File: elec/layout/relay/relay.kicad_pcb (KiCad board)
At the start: 4 copper layers, 6 parts

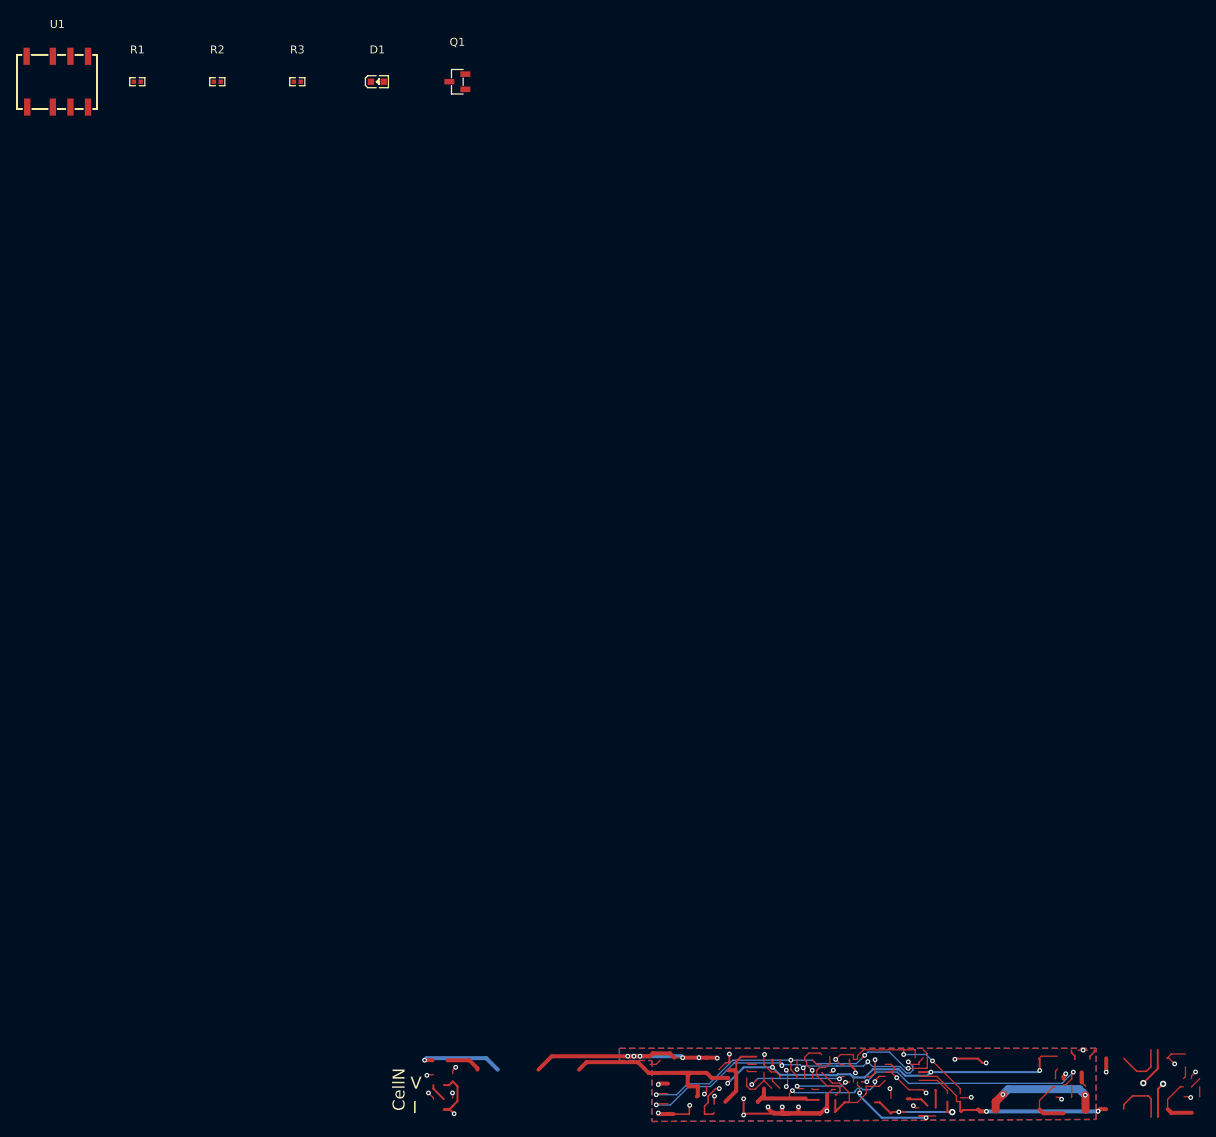
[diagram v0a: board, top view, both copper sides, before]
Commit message: update relay layout
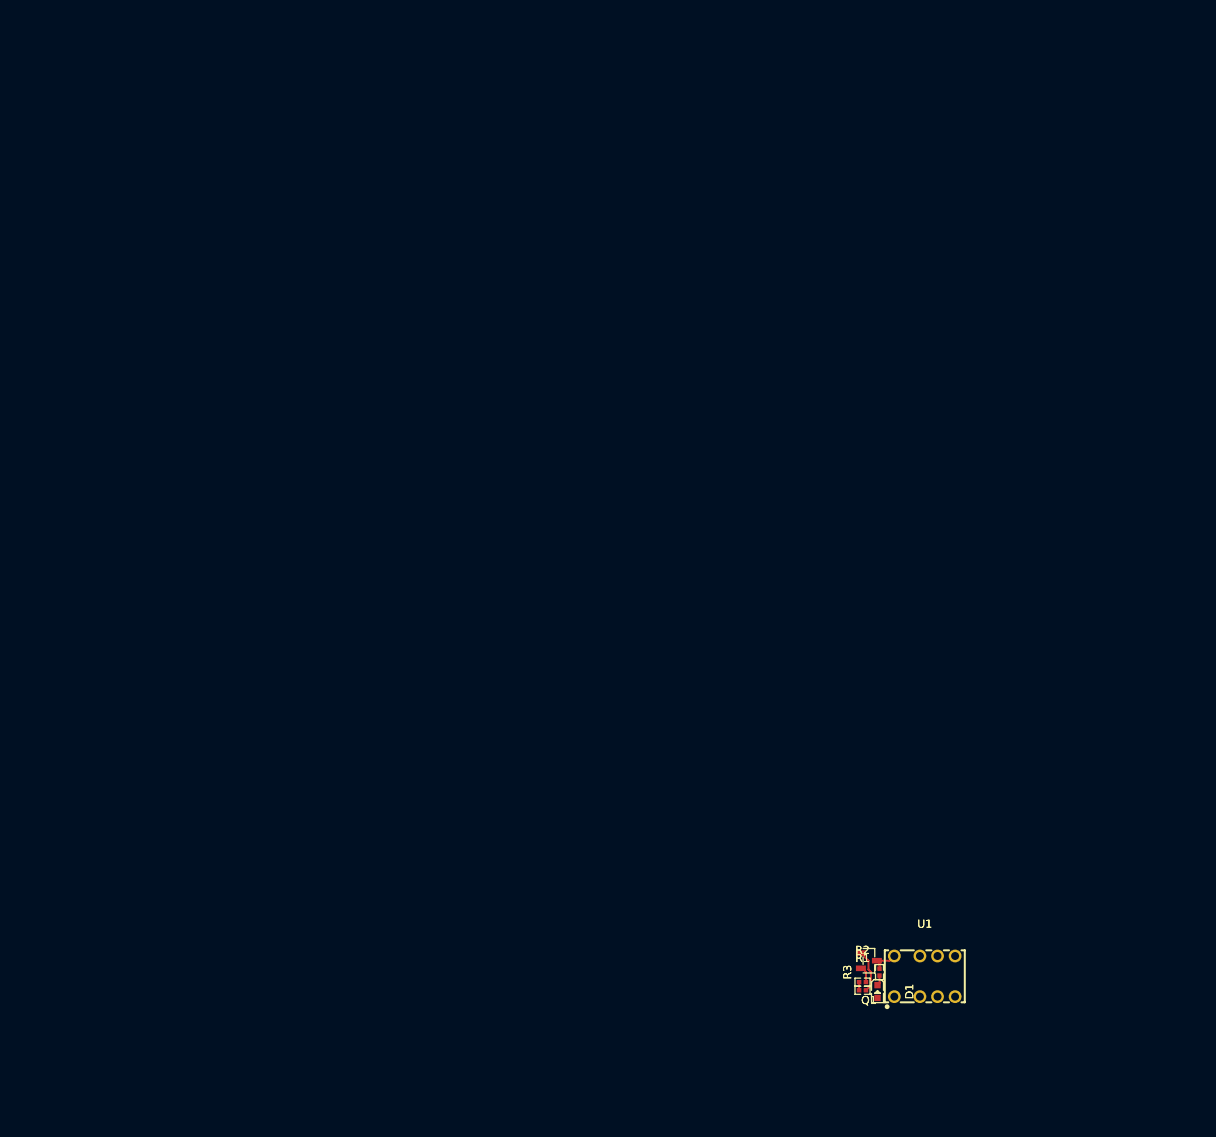
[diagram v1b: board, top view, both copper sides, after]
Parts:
- U1: footprint lib:RELAY-SMD_HFD4-5-SR -> atopile:RELAY-TH_HFDXXX-689a1e
- moved U1 155.8 mm to (118.4, 106.8)
- moved R1 145.3 mm to (110.7, 108.6)
- moved R2 138.5 mm to (110.7, 107.5)
- moved R3 133.0 mm to (112.8, 106.3), turned to 90 degrees
- moved D1 129.8 mm to (112.5, 108.7), turned to -90 degrees
- moved Q1 121.3 mm to (111.5, 104.9), turned to 180 degrees
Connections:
- D1 pad 2: hv -> anode
- Q1 pad 2: gnd-3 -> gnd-2
- Q1 pad 3: gnd-2 -> gnd
- R2 pad 2: gnd-3 -> gnd-2
- R3 pad 2: gnd-2 -> gnd
- U1 pad 1: hv -> anode
- U1 pad 2: (no net) -> relay.footprint.pins[1].net-net
- U1 pad 3: gnd -> gnd-3
- U1 pad 5: hv-2 -> hv
- U1 pad 7: (no net) -> relay.footprint.pins[6].net-net
- U1 pad 8: gnd-2 -> gnd
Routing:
- net (no net): track 617.3 -> 0.00 mm, vias 81 -> 0
- net gate: track 0.00 -> 5.42 mm
- net gnd: track 0.00 -> 3.88 mm
- net gnd-2: track 0.00 -> 2.16 mm
- net cathode: track 0.00 -> 1.30 mm
- net line: track 0.00 -> 1.03 mm
- removed copper zone on B.Cu, net (none)
- removed copper zone on F.Cu, net (none)
- removed copper zone on In1.Cu, net (none)
- removed copper zone on In2.Cu, net (none)
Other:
- board text removed: "CellN"
- board text removed: "I"
- board text removed: "V"

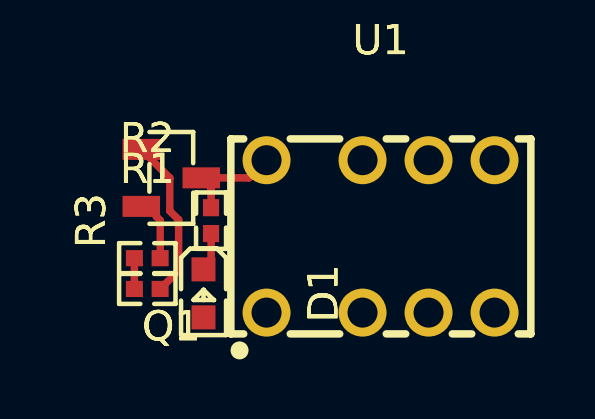
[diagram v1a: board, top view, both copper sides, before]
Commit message: update layouts to kicad 9
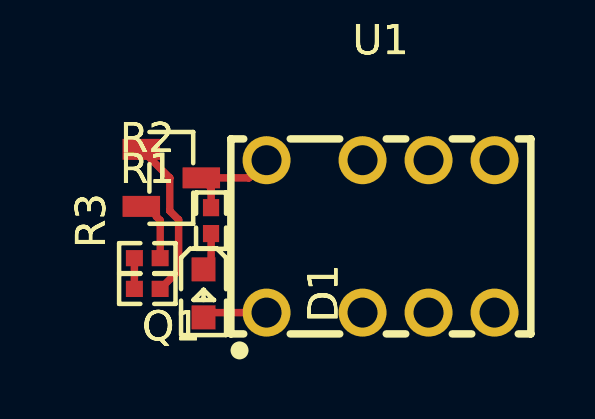
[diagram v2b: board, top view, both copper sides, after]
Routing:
- net anode: track 0.00 -> 2.17 mm

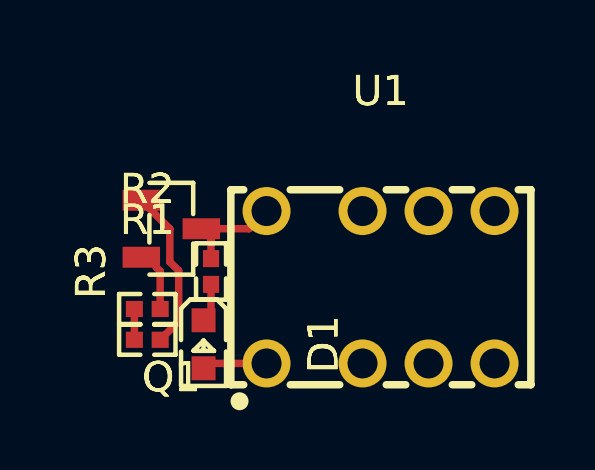
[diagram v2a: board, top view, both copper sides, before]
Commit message: update n-fet part for stock
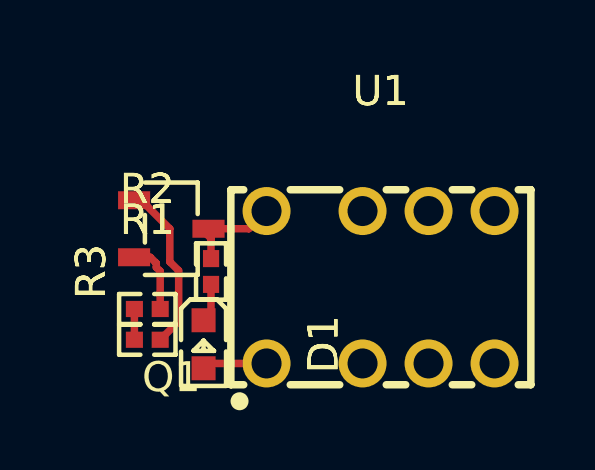
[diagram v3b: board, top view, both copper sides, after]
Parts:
- Q1: footprint atopile:SOT-23-3_L2.9-W1.3-P1.90-LS2.4-BR-688f29 -> atopile:SOT-23-3_L2.9-W1.6-P1.90-LS2.8-BR-186170
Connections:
- Q1 pad 2: gnd-2 -> gnd-1
- R2 pad 2: gnd-2 -> gnd-1
- U1 pad 3: gnd-3 -> gnd-2
- U1 pad 4: gnd-1 -> gnd-3
- U1 pad 5: hv -> hv-1
- U1 pad 6: hv-1 -> hv
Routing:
- net gnd-2: track 2.16 -> 0.00 mm
- net gnd-1: track 0.00 -> 2.16 mm

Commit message: building frozen
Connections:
- D1 pad 2: anode -> hv-1
- Q1 pad 2: gnd-1 -> gnd-2
- Q1 pad 3: gnd -> gnd-1
- R2 pad 2: gnd-1 -> gnd-2
- R3 pad 2: gnd -> gnd-1
- U1 pad 1: anode -> hv-1
- U1 pad 3: gnd-2 -> gnd-3
- U1 pad 4: gnd-3 -> gnd
- U1 pad 5: hv-1 -> hv-2
- U1 pad 8: gnd -> gnd-1
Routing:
- net gnd: track 3.88 -> 0.00 mm
- net hv-1: track 0.00 -> 2.17 mm
- net anode: track 2.17 -> 0.00 mm
- net gnd-2: track 0.00 -> 2.16 mm
- net gnd-1: track 2.16 -> 3.88 mm
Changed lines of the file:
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@@
         (legacy_teardrops no)
     )
-    (paper A4)
+    (paper "A4")
     (layers
         (0 "F.Cu" signal)
@@
         (tenting front back)
         (pcbplotparams
-            (layerselection "0x00000000_00000000_55555555_5755f5ff")
-            (plot_on_all_layers_selection "0x00000000_00000000_00000000_00000000")
+            (layerselection 0x00000000_00000000_55555555_5755f5ff)
+            (plot_on_all_layers_selection 0x00000000_00000000_00000000_00000000)
             (disableapertmacros no)
             (usegerberextensions no)
@@
             (dxfusepcbnewfont yes)
             (psnegative no)
+            (psa4output no)
             (plot_black_and_white yes)
-            (psa4output no)
+            (plotinvisibletext no)
+            (sketchpadsonfab no)
             (plotreference yes)
+            (plotvalue yes)
             (plotpadnumbers no)
             (hidednponfab no)
             (sketchdnponfab yes)
             (crossoutdnponfab yes)
-            (plotvalue yes)
             (plotfptext yes)
-            (plotinvisibletext no)
-            (sketchpadsonfab no)
             (subtractmaskfromsilk no)
             (outputformat 1)
@@
     )
     (net 0 "")
-    (net 1 "gnd-3")
-    (net 2 "gnd-1")
+    (net 1 "gnd")
+    (net 2 "gnd-2")
     (net 3 "hv")
-    (net 4 "gnd-2")
-    (net 5 "hv-1")
+    (net 4 "gnd-3")
+    (net 5 "hv-2")
     (net 6 "cathode")
-    (net 7 "gnd")
-    (net 8 "anode")
+    (net 7 "gnd-1")
+    (net 8 "hv-1")
     (net 9 "gate")
     (net 10 "line")
@@
             (size 0.57 0.54)
             (layers "F.Cu" "F.Mask" "F.Paste")
-            (net 2 "gnd-1")
+            (net 2 "gnd-2")
             (remove_unused_layers yes)
             (keep_end_layers yes)
@@
             (size 0.57 0.54)
             (layers "F.Cu" "F.Mask" "F.Paste")
-            (net 7 "gnd")
+            (net 7 "gnd-1")
             (remove_unused_layers yes)
             (keep_end_layers yes)
@@
             (size 0.8 0.8)
             (layers "F.Cu" "F.Mask" "F.Paste")
-            (net 8 "anode")
+            (net 8 "hv-1")
             (remove_unused_layers yes)
             (keep_end_layers yes)
@@
             (drill 0.999998)
             (layers "*.Cu" "*.Mask")
-            (net 8 "anode")
+            (net 8 "hv-1")
             (remove_unused_layers no)
             (keep_end_layers yes)
@@
             (drill 0.999998)
             (layers "*.Cu" "*.Mask")
-            (net 4 "gnd-2")
+            (net 4 "gnd-3")
             (remove_unused_layers no)
             (keep_end_layers yes)
@@
             (drill 0.999998)
             (layers "*.Cu" "*.Mask")
-            (net 1 "gnd-3")
+            (net 1 "gnd")
             (remove_unused_layers no)
             (keep_end_layers yes)
@@
             (drill 0.999998)
             (layers "*.Cu" "*.Mask")
-            (net 5 "hv-1")
+            (net 5 "hv-2")
             (remove_unused_layers no)
             (keep_end_layers yes)
@@
             (drill 0.999998)
             (layers "*.Cu" "*.Mask")
-            (net 7 "gnd")
+            (net 7 "gnd-1")
             (remove_unused_layers no)
             (keep_end_layers yes)
@@
             (size 1.07 0.6)
             (layers "F.Cu" "F.Paste" "F.Mask")
-            (net 2 "gnd-1")
+            (net 2 "gnd-2")
             (remove_unused_layers yes)
             (keep_end_layers yes)
@@
             (size 1.07 0.6)
             (layers "F.Cu" "F.Paste" "F.Mask")
-            (net 7 "gnd")
+            (net 7 "gnd-1")
             (remove_unused_layers yes)
             (keep_end_layers yes)

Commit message: Build everything with ordered params to fix frozen builds
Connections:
- Q1 pad 2: gnd-2 -> gnd
- R2 pad 2: gnd-2 -> gnd
- U1 pad 4: gnd -> gnd-2
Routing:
- net gnd-2: track 2.16 -> 0.00 mm
- net gnd: track 0.00 -> 2.16 mm
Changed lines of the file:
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@@
     )
     (net 0 "")
-    (net 1 "gnd")
-    (net 2 "gnd-2")
+    (net 1 "gnd-2")
+    (net 2 "gnd")
     (net 3 "hv")
     (net 4 "gnd-3")
@@
             )
         )
+        (property "PARAM_max_power" "{\"type\": \"Quantity_Set_Discrete\", \"data\": {\"intervals\": {\"type\": \"Numeric_Interval_Disjoint\", \"data\": {\"intervals\": [{\"type\": \"Numeric_Interval\", \"data\": {\"min\": 0.0625, \"max\": 0.0625}}]}}, \"unit\": \"watt\"}}"
+            (at 0 0 0)
+            (layer "User.9")
+            (hide yes)
+            (effects
+                (font
+                    (size 0.125 0.125)
+                    (thickness 0.01875)
+                )
+            )
+        )
+        (property "PARAM_resistance" "{\"type\": \"Quantity_Interval_Disjoint\", \"data\": {\"intervals\": {\"type\": \"Numeric_Interval_Disjoint\", \"data\": {\"intervals\": [{\"type\": \"Numeric_Interval\", \"data\": {\"min\": 990.0000002235174, \"max\": 1009.9999997764826}}]}}, \"unit\": \"ohm\"}}"
+            (at 0 0 0)
+            (layer "User.9")
+            (hide yes)
+            (effects
+                (font
+                    (size 0.125 0.125)
+                    (thickness 0.01875)
+                )
+            )
+        )
+        (property "PARAM_max_voltage" "{\"type\": \"Quantity_Set_Discrete\", \"data\": {\"intervals\": {\"type\": \"Numeric_Interval_Disjoint\", \"data\": {\"intervals\": [{\"type\": \"Numeric_Interval\", \"data\": {\"min\": 50.0, \"max\": 50.0}}]}}, \"unit\": \"volt\"}}"
+            (at 0 0 0)
+            (layer "User.9")
+            (hide yes)
+            (effects
+                (font
+                    (size 0.125 0.125)
+                    (thickness 0.01875)
+                )
+            )
+        )
         (attr smd)
         (fp_line
@@
             (size 0.57 0.54)
             (layers "F.Cu" "F.Mask" "F.Paste")
-            (net 2 "gnd-2")
+            (net 2 "gnd")
             (remove_unused_layers yes)
             (keep_end_layers yes)
@@
             )
         )
+        (property "PARAM_max_power" "{\"type\": \"Quantity_Set_Discrete\", \"data\": {\"intervals\": {\"type\": \"Numeric_Interval_Disjoint\", \"data\": {\"intervals\": [{\"type\": \"Numeric_Interval\", \"data\": {\"min\": 0.0625, \"max\": 0.0625}}]}}, \"unit\": \"watt\"}}"
+            (at 0 0 0)
+            (layer "User.9")
+            (hide yes)
+            (effects
+                (font
+                    (size 0.125 0.125)
+                    (thickness 0.01875)
+                )
+            )
+        )
+        (property "PARAM_resistance" "{\"type\": \"Quantity_Interval_Disjoint\", \"data\": {\"intervals\": {\"type\": \"Numeric_Interval_Disjoint\", \"data\": {\"intervals\": [{\"type\": \"Numeric_Interval\", \"data\": {\"min\": 9900.000002235174, \"max\": 10099.999997764826}}]}}, \"unit\": \"ohm\"}}"
+            (at 0 0 0)
+            (layer "User.9")
+            (hide yes)
+            (effects
+                (font
+                    (size 0.125 0.125)
+                    (thickness 0.01875)
+                )
+            )
+        )
+        (property "PARAM_max_voltage" "{\"type\": \"Quantity_Set_Discrete\", \"data\": {\"intervals\": {\"type\": \"Numeric_Interval_Disjoint\", \"data\": {\"intervals\": [{\"type\": \"Numeric_Interval\", \"data\": {\"min\": 50.0, \"max\": 50.0}}]}}, \"unit\": \"volt\"}}"
+            (at 0 0 0)
+            (layer "User.9")
+            (hide yes)
+            (effects
+                (font
+                    (size 0.125 0.125)
+                    (thickness 0.01875)
+                )
+            )
+        )
         (attr smd)
         (fp_line
@@
             )
         )
+        (property "PARAM_max_power" "{\"type\": \"Quantity_Set_Discrete\", \"data\": {\"intervals\": {\"type\": \"Numeric_Interval_Disjoint\", \"data\": {\"intervals\": [{\"type\": \"Numeric_Interval\", \"data\": {\"min\": 0.0625, \"max\": 0.0625}}]}}, \"unit\": \"watt\"}}"
+            (at 0 0 0)
+            (layer "User.9")
+            (hide yes)
+            (effects
+                (font
+                    (size 0.125 0.125)
+                    (thickness 0.01875)
+                )
+            )
+        )
+        (property "PARAM_resistance" "{\"type\": \"Quantity_Interval_Disjoint\", \"data\": {\"intervals\": {\"type\": \"Numeric_Interval_Disjoint\", \"data\": {\"intervals\": [{\"type\": \"Numeric_Interval\", \"data\": {\"min\": 990.0000002235174, \"max\": 1009.9999997764826}}]}}, \"unit\": \"ohm\"}}"
+            (at 0 0 0)
+            (layer "User.9")
+            (hide yes)
+            (effects
+                (font
+                    (size 0.125 0.125)
+                    (thickness 0.01875)
+                )
+            )
+        )
+        (property "PARAM_max_voltage" "{\"type\": \"Quantity_Set_Discrete\", \"data\": {\"intervals\": {\"type\": \"Numeric_Interval_Disjoint\", \"data\": {\"intervals\": [{\"type\": \"Numeric_Interval\", \"data\": {\"min\": 50.0, \"max\": 50.0}}]}}, \"unit\": \"volt\"}}"
+            (at 0 0 0)
+            (layer "User.9")
+            (hide yes)
+            (effects
+                (font
+                    (size 0.125 0.125)
+                    (thickness 0.01875)
+                )
+            )
+        )
         (attr smd)
         (fp_line
@@
             (drill 0.999998)
             (layers "*.Cu" "*.Mask")
-            (net 1 "gnd")
+            (net 1 "gnd-2")
             (remove_unused_layers no)
             (keep_end_layers yes)
@@
             (size 1.07 0.6)
             (layers "F.Cu" "F.Paste" "F.Mask")
-            (net 2 "gnd-2")
+            (net 2 "gnd")
             (remove_unused_layers yes)
             (keep_end_layers yes)

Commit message: Cleanup layout for usb hub and usb-uart, add CM5 controller heatsink outline
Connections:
- D1 pad 2: hv-1 -> hv-2
- U1 pad 1: hv-1 -> hv-2
- U1 pad 5: hv-2 -> hv-1
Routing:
- net hv-2: track 0.00 -> 2.17 mm
- net hv-1: track 2.17 -> 0.00 mm
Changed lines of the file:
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@@
     (net 3 "hv")
     (net 4 "gnd-3")
-    (net 5 "hv-2")
+    (net 5 "hv-1")
     (net 6 "cathode")
     (net 7 "gnd-1")
-    (net 8 "hv-1")
+    (net 8 "hv-2")
     (net 9 "gate")
     (net 10 "line")
@@
             (size 0.8 0.8)
             (layers "F.Cu" "F.Mask" "F.Paste")
-            (net 8 "hv-1")
+            (net 8 "hv-2")
             (remove_unused_layers yes)
             (keep_end_layers yes)
@@
             (drill 0.999998)
             (layers "*.Cu" "*.Mask")
-            (net 8 "hv-1")
+            (net 8 "hv-2")
             (remove_unused_layers no)
             (keep_end_layers yes)
@@
             (drill 0.999998)
             (layers "*.Cu" "*.Mask")
-            (net 5 "hv-2")
+            (net 5 "hv-1")
             (remove_unused_layers no)
             (keep_end_layers yes)

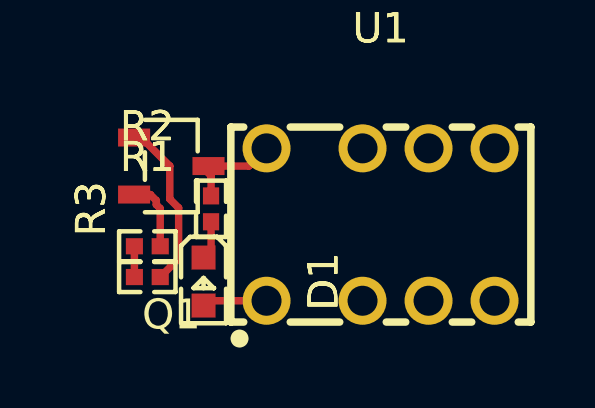
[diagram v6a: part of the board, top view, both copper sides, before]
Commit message: update address pin on analog out, update led value on relay
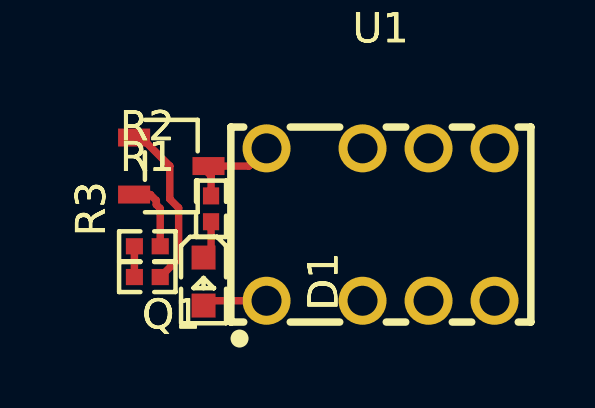
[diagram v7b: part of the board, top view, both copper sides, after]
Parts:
- R3: value 1kΩ ±1% 62.5mW -> 2kΩ ±1% 62.5mW
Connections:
- net hv-2 renamed anode
- Q1 pad 2: gnd -> gnd-3
- R2 pad 2: gnd -> gnd-3
- U1 pad 3: gnd-3 -> gnd-2
- U1 pad 4: gnd-2 -> gnd
- U1 pad 5: hv-1 -> hv
- U1 pad 6: hv -> hv-1
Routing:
- net gnd-3: track 0.00 -> 2.16 mm
- net gnd: track 2.16 -> 0.00 mm

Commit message: checkin
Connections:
- D1 pad 2: anode -> hv
- Q1 pad 2: gnd-3 -> gnd-2
- R2 pad 2: gnd-3 -> gnd-2
- U1 pad 1: anode -> hv
- U1 pad 3: gnd-2 -> gnd
- U1 pad 4: gnd -> gnd-3
- U1 pad 5: hv -> hv-1
- U1 pad 6: hv-1 -> hv-2
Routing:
- net hv: track 0.00 -> 2.17 mm
- net anode: track 2.17 -> 0.00 mm
- net gnd-3: track 2.16 -> 0.00 mm
- net gnd-2: track 0.00 -> 2.16 mm
